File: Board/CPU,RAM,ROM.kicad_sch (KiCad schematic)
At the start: 25 parts, among them IC3 74LVC125, IC6 741G04DBV, IC7 74LVC138, U1 IS61C5128AL-10TLI, X3 SG-8002CE

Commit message: more work on r2.1a - only bom xls is missing/outdated
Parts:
- D9: value 1N4148 -> 1N4448
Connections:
- net RAMD0: now also U$2.67 (IO_L2P_CMPCLK_2); no longer U$2.69 (IO_L1N_M0_CMPMISO_2)
- net RAMD7: now also U$2.69 (IO_L1N_M0_CMPMISO_2); no longer U$2.75 (IO_L74P_AWAKE_1)
- net SPI_IN3: now also U$2.75 (IO_L74P_AWAKE_1); no longer U$2.67 (IO_L2P_CMPCLK_2)
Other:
- note added: "CSA-ULTRACPU-V2.1A-20241215"
- note removed: "CSA-ULTRACPU-V2.1A-20241207"
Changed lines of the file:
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@@
 		)
 	)
-	(wire
-		(pts
-			(xy 370.84 157.48) (xy 370.84 198.12)
-		)
-		(stroke
-			(width 0.1524)
-			(type solid)
-		)
-	)
 	(bus
 		(pts
@@
 	(wire
 		(pts
+			(xy 355.6 157.48) (xy 355.6 189.23)
+		)
+		(stroke
+			(width 0.1524)
+			(type solid)
+		)
+	)
+	(wire
+		(pts
 			(xy 175.26 281.94) (xy 182.88 281.94)
 		)
@@
 	(wire
 		(pts
-			(xy 370.84 73.66) (xy 378.46 73.66)
-		)
-		(stroke
-			(width 0.1524)
-			(type solid)
-		)
-	)
-	(wire
-		(pts
 			(xy 513.08 121.92) (xy 530.86 121.92)
 		)
@@
 	(wire
 		(pts
-			(xy 368.3 157.48) (xy 368.3 189.23)
-		)
-		(stroke
-			(width 0)
-			(type default)
-		)
-	)
-	(wire
-		(pts
 			(xy 73.66 33.02) (xy 93.98 33.02)
 		)
@@
 	(wire
 		(pts
+			(xy 370.84 157.48) (xy 370.84 189.23)
+		)
+		(stroke
+			(width 0.1524)
+			(type solid)
+		)
+	)
+	(wire
+		(pts
 			(xy 464.82 185.42) (xy 477.52 185.42)
 		)
@@
 	(wire
 		(pts
-			(xy 370.84 81.28) (xy 370.84 73.66)
+			(xy 370.84 49.53) (xy 370.84 81.28)
 		)
 		(stroke
@@
 	(wire
 		(pts
+			(xy 368.3 58.42) (xy 368.3 81.28)
+		)
+		(stroke
+			(width 0)
+			(type default)
+		)
+	)
+	(wire
+		(pts
 			(xy 444.5 121.92) (xy 444.5 124.46)
 		)
@@
 	(wire
 		(pts
+			(xy 358.14 157.48) (xy 358.14 189.23)
+		)
+		(stroke
+			(width 0.1524)
+			(type solid)
+		)
+	)
+	(wire
+		(pts
 			(xy 528.32 93.98) (xy 528.32 55.88)
 		)
@@
 	(wire
 		(pts
-			(xy 358.14 205.74) (xy 358.14 157.48)
-		)
-		(stroke
-			(width 0.1524)
-			(type solid)
-		)
-	)
-	(wire
-		(pts
 			(xy 332.74 71.12) (xy 332.74 48.26)
 		)
@@
 	(wire
 		(pts
-			(xy 378.46 45.72) (xy 378.46 73.66)
-		)
-		(stroke
-			(width 0.1524)
-			(type solid)
-		)
-	)
-	(wire
-		(pts
 			(xy 45.72 35.56) (xy 40.64 35.56)
 		)
@@
 	(wire
 		(pts
-			(xy 355.6 157.48) (xy 355.6 205.74)
-		)
-		(stroke
-			(width 0.1524)
-			(type solid)
-		)
-	)
-	(wire
-		(pts
 			(xy 444.5 129.54) (xy 444.5 132.08)
 		)
@@
 	(wire
 		(pts
-			(xy 363.22 193.04) (xy 363.22 157.48)
-		)
-		(stroke
-			(width 0.1524)
-			(type solid)
-		)
-	)
-	(wire
-		(pts
 			(xy 121.92 271.78) (xy 144.78 271.78)
 		)
@@
 	(wire
 		(pts
-			(xy 368.3 58.42) (xy 368.3 81.28)
-		)
-		(stroke
-			(width 0)
-			(type default)
-		)
-	)
-	(wire
-		(pts
 			(xy 144.78 254) (xy 132.08 254)
 		)
@@
 		)
 	)
+	(wire
+		(pts
+			(xy 368.3 157.48) (xy 368.3 189.23)
+		)
+		(stroke
+			(width 0)
+			(type default)
+		)
+	)
 	(bus
 		(pts
@@
 	(wire
 		(pts
+			(xy 363.22 157.48) (xy 363.22 189.23)
+		)
+		(stroke
+			(width 0)
+			(type default)
+		)
+	)
+	(wire
+		(pts
 			(xy 52.07 278.13) (xy 52.07 275.59)
 		)
@@
 		)
 	)
-	(text "CSA-ULTRACPU-V2.1A-20241207"
+	(text "CSA-ULTRACPU-V2.1A-20241215"
 		(exclude_from_sim no)
 		(at 441.96 325.12 0)
@@
 	(global_label "SPI_IN3"
 		(shape bidirectional)
-		(at 363.22 190.5 90)
+		(at 368.3 58.42 90)
 		(fields_autoplaced yes)
 		(effects
@@
 		)
 		(property "Intersheetrefs" "${INTERSHEET_REFS}"
-			(at 363.22 179.433 90)
+			(at 368.3 47.353 90)
 			(effects
 				(font
@@
 	(global_label "RAMD7"
 		(shape bidirectional)
-		(at 368.3 58.42 90)
+		(at 368.3 189.23 270)
 		(fields_autoplaced yes)
 		(effects
@@
 				(size 1.2446 1.2446)
 			)
-			(justify left)
+			(justify right)
 		)
 		(property "Intersheetrefs" "${INTERSHEET_REFS}"
-			(at 368.3 48.2421 90)
+			(at 368.3 199.4079 90)
 			(effects
 				(font
 					(size 1.27 1.27)
 				)
-				(justify left)
+				(justify right)
 				(hide yes)
 			)
@@
 	(global_label "SPI_MOSI"
 		(shape bidirectional)
-		(at 355.6 187.96 90)
+		(at 355.6 189.23 270)
 		(fields_autoplaced yes)
 		(effects
@@
 				(size 1.2446 1.2446)
 			)
-			(justify left)
+			(justify right)
 		)
 		(property "Intersheetrefs" "${INTERSHEET_REFS}"
-			(at 355.6 175.4706 90)
+			(at 355.6 201.7194 90)
 			(effects
 				(font
 					(size 1.27 1.27)
 				)
-				(justify left)
+				(justify right)
 				(hide yes)
 			)
@@
 	(global_label "RAMD0"
 		(shape bidirectional)
-		(at 368.3 189.23 270)
+		(at 363.22 189.23 270)
 		(fields_autoplaced yes)
 		(effects
@@
 		)
 		(property "Intersheetrefs" "${INTERSHEET_REFS}"
-			(at 368.3 199.4079 90)
+			(at 363.22 199.4079 90)
 			(effects
 				(font
@@
 	(global_label "SPI_CLK/CCLK"
 		(shape bidirectional)
-		(at 370.84 190.5 90)
+		(at 370.84 189.23 270)
 		(fields_autoplaced yes)
 		(effects
@@
 				(size 1.2446 1.2446)
 			)
-			(justify left)
+			(justify right)
 		)
 		(property "Intersheetrefs" "${INTERSHEET_REFS}"
-			(at 370.84 172.973 90)
+			(at 370.84 206.757 90)
 			(effects
 				(font
 					(size 1.27 1.27)
 				)
-				(justify left)
+				(justify right)
 				(hide yes)
 			)
@@
 	(global_label "IGOUT"
 		(shape bidirectional)
-		(at 378.46 63.5 90)
+		(at 370.84 49.53 270)
 		(fields_autoplaced yes)
 		(effects
@@
 				(size 1.2446 1.2446)
 			)
-			(justify left)
+			(justify right)
 		)
 		(property "Intersheetrefs" "${INTERSHEET_REFS}"
-			(at 378.46 54.0924 90)
+			(at 370.84 58.9376 90)
 			(effects
 				(font
 					(size 1.27 1.27)
 				)
-				(justify left)
+				(justify right)
 				(hide yes)
 			)
@@
 	(global_label "SPI_MISO/DIN"
 		(shape bidirectional)
-		(at 358.14 190.5 90)
+		(at 358.14 189.23 270)
 		(fields_autoplaced yes)
 		(effects
@@
 				(size 1.2446 1.2446)
 			)
-			(justify left)
+			(justify right)
 		)
 		(property "Intersheetrefs" "${INTERSHEET_REFS}"
-			(at 358.14 173.5655 90)
+			(at 358.14 206.1645 90)
 			(effects
 				(font
 					(size 1.27 1.27)
 				)
-				(justify left)
+				(justify right)
 				(hide yes)
 			)
@@
 			)
 		)
-		(property "Value" "1N4148"
+		(property "Value" "1N4448"
 			(at 414.02 136.9314 0)
 			(effects

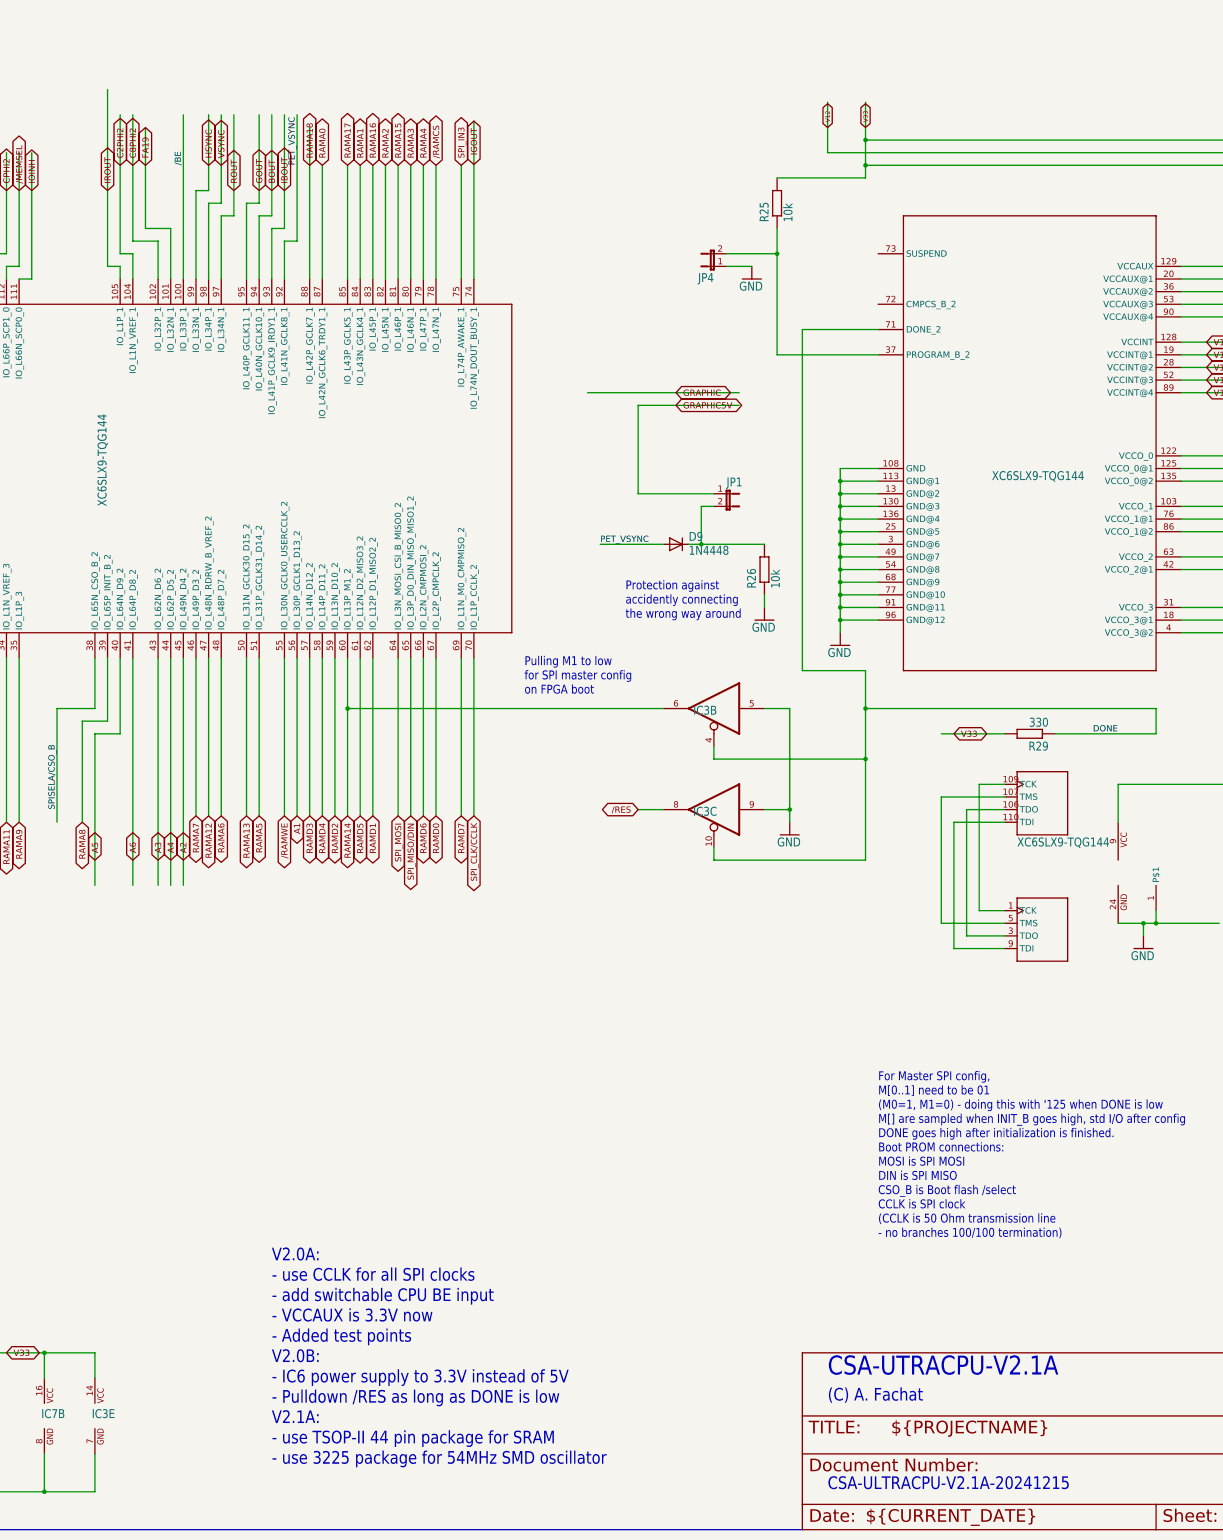
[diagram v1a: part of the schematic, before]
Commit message: start r2.2a, moving from VGA to HDMI
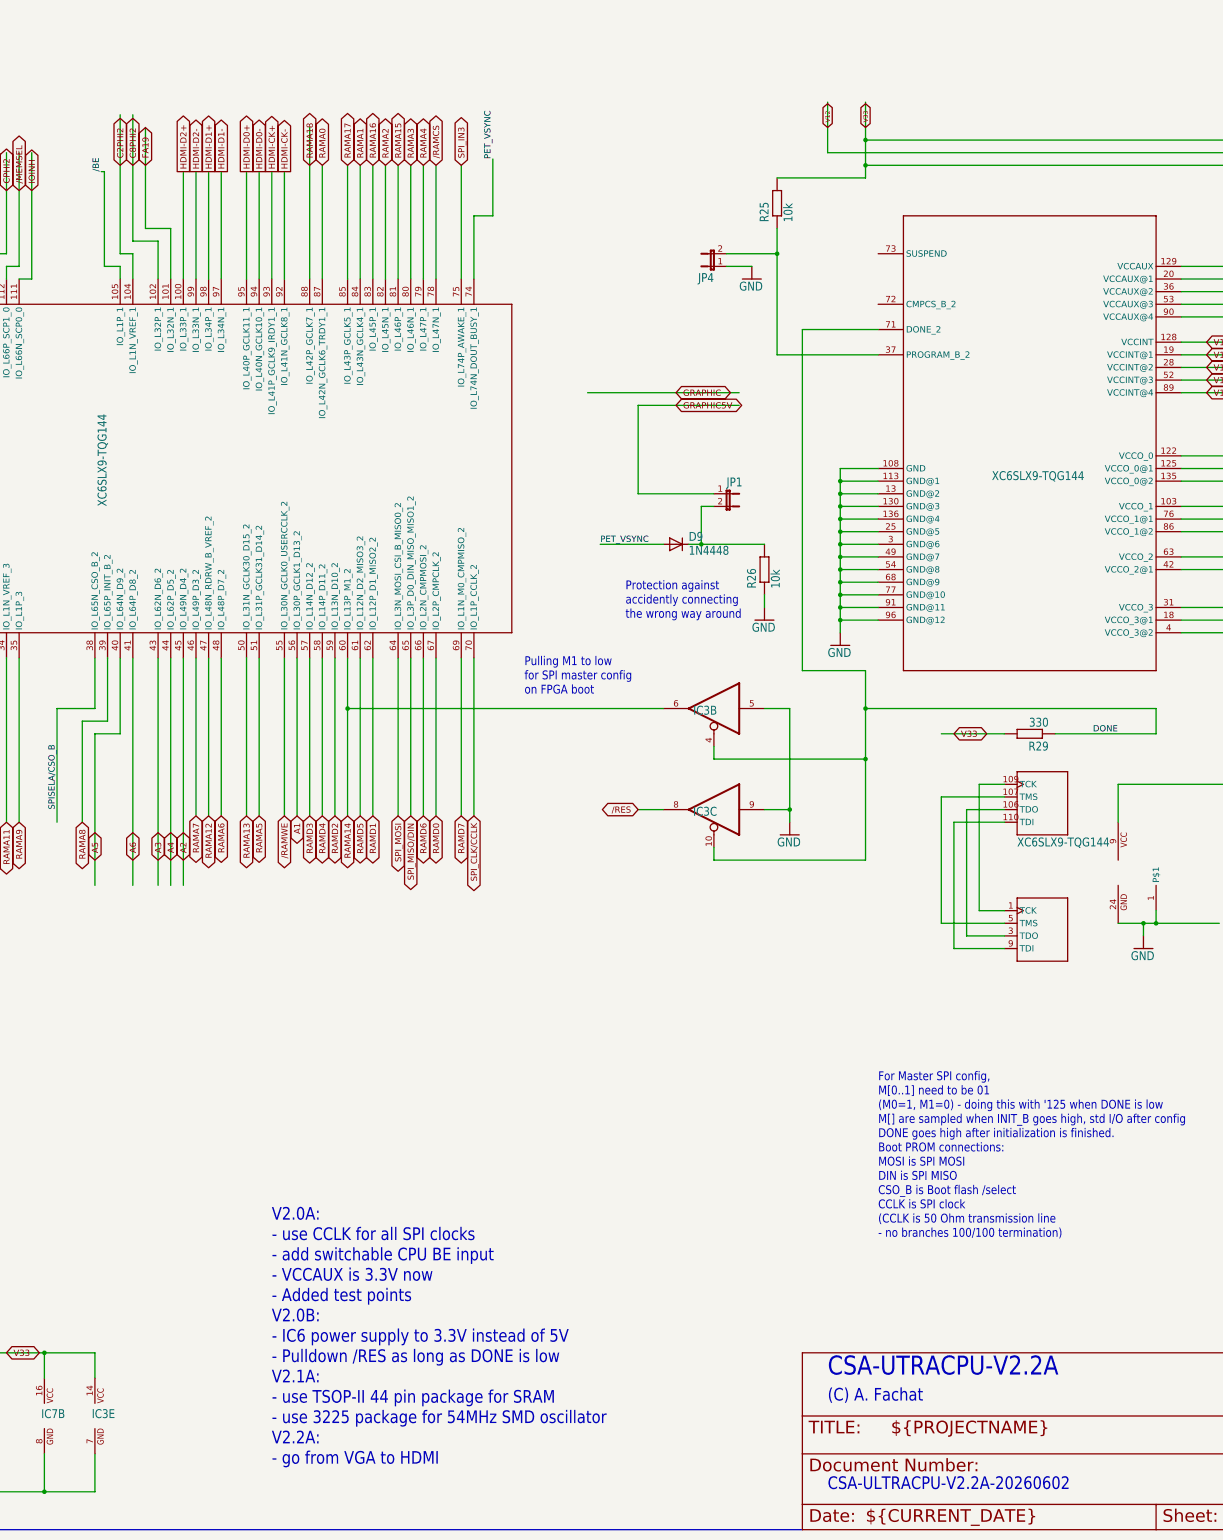
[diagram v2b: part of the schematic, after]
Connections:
- net IGOUT is gone; now on net PET_VSYNC: U$2.74 (IO_L74N_DOUT_BUSY_1)
- net IROUT is gone; now on net /BE: U$2.105 (IO_L1P_1)
- net /BE: no longer U$2.100 (IO_L33P_1)
- net PET_VSYNC: no longer U$2.92 (IO_L41N_GCLK8_1)
- net BOUT renamed HDMI-D0-
- net GOUT renamed HDMI-D0+
- net HSYNC renamed HDMI-D2-
- net IBOUT renamed HDMI-CK+
- net ROUT renamed HDMI-D1-
- net VSYNC renamed HDMI-D1+
- new net HDMI-CK-: U$2.92 (IO_L41N_GCLK8_1)
- new net HDMI-D2+: U$2.100 (IO_L33P_1)
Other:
- note added: "CSA-ULTRACPU-V2.2A-20260602"
- note added: "CSA-UTRACPU-V2.2A"
- note added: "V2.0A: - use CCLK for all SPI clocks - add switchable CPU BE input - VCCAUX is 3.3V now - Added test points V2.0B: - IC6 power supply to 3.3V instead of 5V - Pulldown /RES as long as DONE is low V2.1A: - use TSOP-II 44 pin package for SRAM - use 3225 package for 54MHz SMD oscillator V2.2A: - go from VGA to HDMI"
- note removed: "CSA-ULTRACPU-V2.1A-20241215"
- note removed: "CSA-UTRACPU-V2.1A"
- note removed: "V2.0A: - use CCLK for all SPI clocks - add switchable CPU BE input - VCCAUX is 3.3V now - Added test points V2.0B: - IC6 power supply to 3.3V instead of 5V - Pulldown /RES as long as DONE is low V2.1A: - use TSOP-II 44 pin package for SRAM - use 3225 package for 54MHz SMD oscillator"
